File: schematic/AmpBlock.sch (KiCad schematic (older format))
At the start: 12 parts

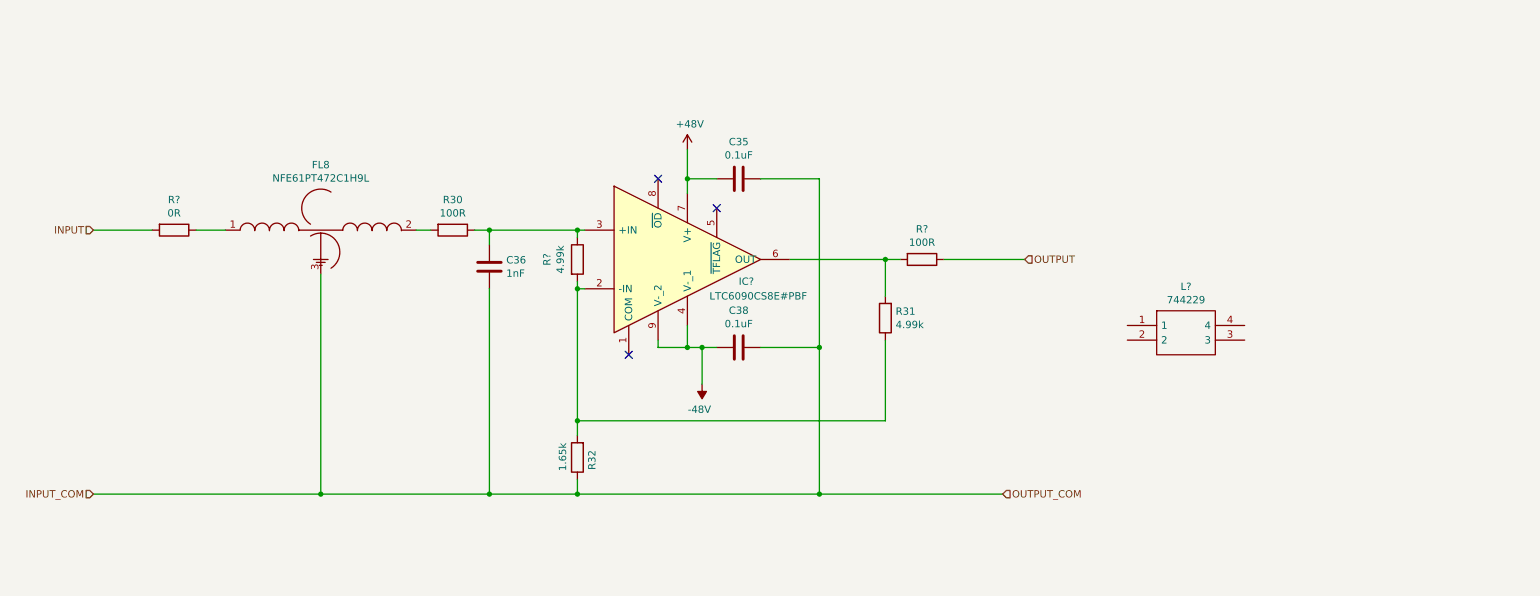
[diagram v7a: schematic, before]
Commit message: finalize schematic and start organizing components in layout
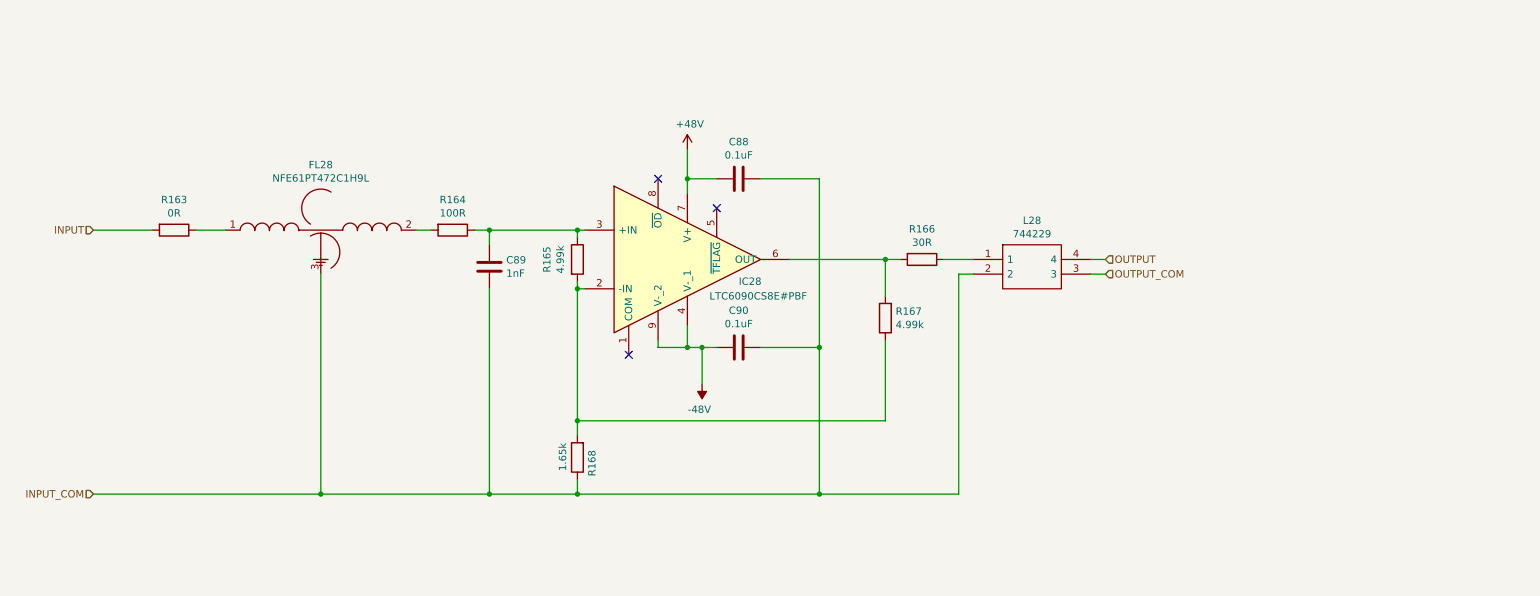
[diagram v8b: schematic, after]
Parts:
- IC8: renamed from IC?; footprint SOIC127P599X175-9N -> ARTIQAmp:SOIC127P599X175-9N
- L8: renamed from L?; footprint WE-SL575 -> ARTIQAmp:WE-SL2
- R46: renamed from R?; value 100R -> 30R
- gave numbers to parts that had none: 2
- renumbered C35 to C28, C36 to C29, C38 to C30, R30 to R44, R31 to R47, R32 to R48
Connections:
- net INPUT_COM: now also L8.2
- net OUTPUT: now also L8.4; no longer R46.1
- net at L8.1: now also R46.1
- net OUTPUT_COM: now reaches L8.3
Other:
- moved on the sheet: L28
